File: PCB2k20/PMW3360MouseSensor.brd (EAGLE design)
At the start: 27 x 21 mm, 10 parts

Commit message: Make the screws not hit the lens
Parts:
- moved C3 4.49 mm to (20.6, 21.2)
- moved C4 4.49 mm to (23.1, 21.2)
- moved R3 4.49 mm to (13.0, 21.2)
- moved U$2 4.49 mm to (10.4, 13.0)
- moved R1 4.49 mm to (18.0, 21.2)
- moved R2 4.49 mm to (15.5, 21.2)
- moved U$1 3.42 mm to (3.43, 14.9)
- moved C2 3.42 mm to (2.79, 11.0)
- moved C1 3.42 mm to (5.33, 11.0)
- moved J1 3.17 mm to (4.70, 1.52)
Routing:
- net 3.3V: track 28.9 -> 34.8 mm
- net NRESET: track 21.5 -> 27.4 mm
- net N$42: track 39.1 -> 42.8 mm
- net N$46: track 3.89 -> 7.07 mm
- net N$47: track 3.83 -> 7.01 mm
- net N$45: track 4.69 -> 7.64 mm
- net N$40: track 6.21 -> 8.49 mm
- net 1.8V: track 22.5 -> 24.4 mm
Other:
- board size 27 x 21 mm -> 34.6 x 24 mm
- board text added: "todo: pin 1 marking pin label"

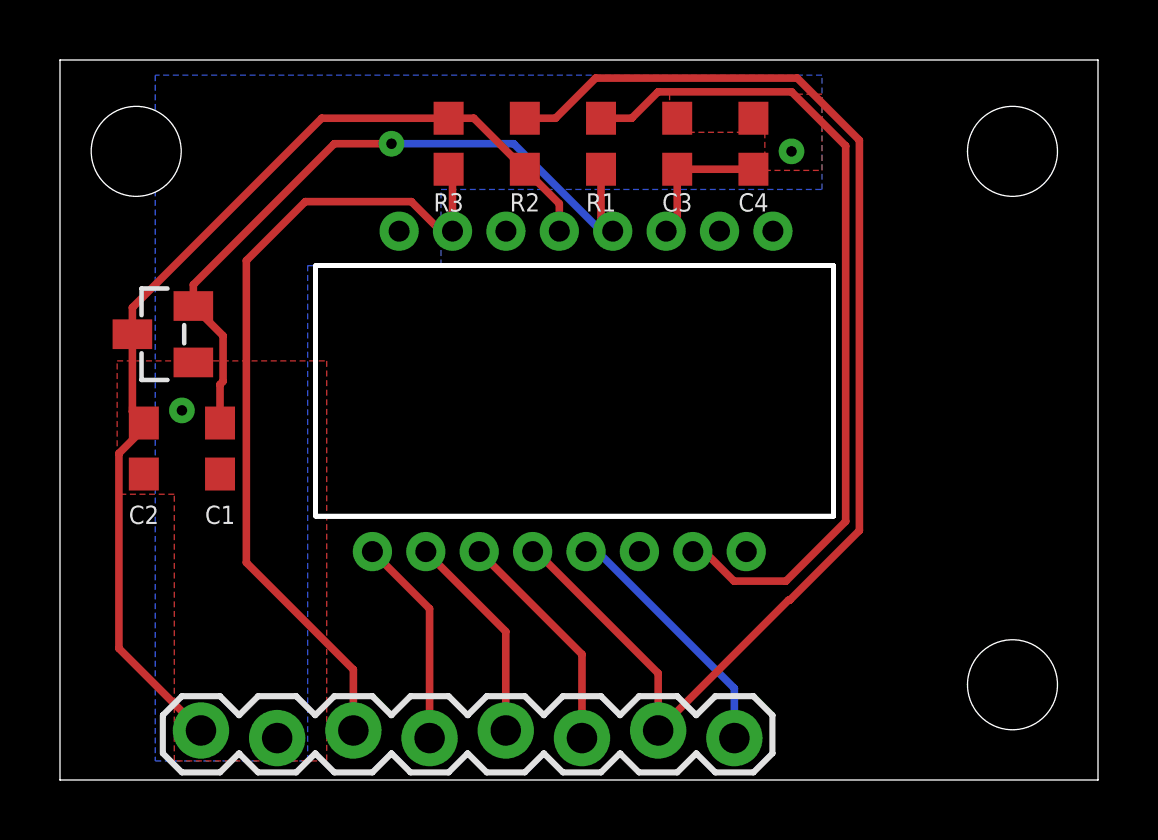
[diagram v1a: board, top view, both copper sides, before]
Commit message: Finalise PMW3360 breakout - done pin markings and cleanup - swapped position of some pins to route stuff more easily
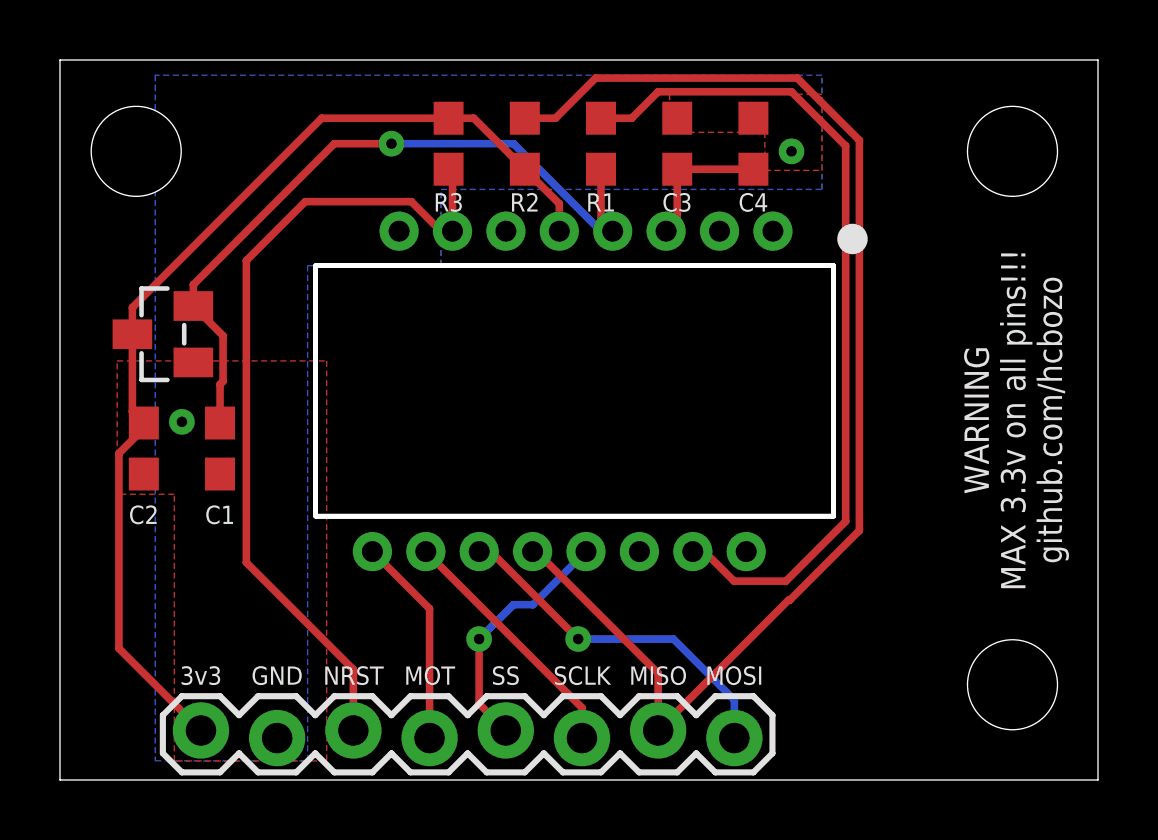
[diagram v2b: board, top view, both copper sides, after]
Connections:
- net N$42 renamed MISO
- net N$47 renamed MOT
- removed net N$40: J1.8, U$2.P13
- removed net N$45: J1.6, U$2.P11
- removed net N$46: J1.5, U$2.P10
- new net MOSI: J1.8, U$2.P11
- new net SCK: J1.6, U$2.P10
- new net SS: J1.5, U$2.P13
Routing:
- net MOSI: track 0.00 -> 11.8 mm, vias 0 -> 1
- net N$40: track 8.49 -> 0.00 mm
- net SCK: track 0.00 -> 8.37 mm
- net SS: track 0.00 -> 8.19 mm, vias 0 -> 1
- net N$45: track 7.64 -> 0.00 mm
- net N$46: track 7.07 -> 0.00 mm
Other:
- board text added: "3v3"
- board text added: "GND"
- board text added: "MISO"
- board text added: "MOSI"
- board text added: "MOT"
- board text added: "NRST"
- board text added: "SCLK"
- board text added: "SS"
- board text added: "WARNING MAX 3.3v on all pins!!! github.com/hcbozo"
- board text removed: "todo: pin 1 marking pin label"

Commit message: add gerbers, please everything turn out well!
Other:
- board text added: "WARNING MAX 3.3v on all pins!!! github.com/hcbozo PMW3360 Breakout"
- board text removed: "WARNING MAX 3.3v on all pins!!! github.com/hcbozo"
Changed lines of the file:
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@@
 <text x="33.401" y="12" size="0.8128" layer="21" font="vector" ratio="16" rot="R90" align="bottom-center">WARNING
 MAX 3.3v on all pins!!!
-github.com/hcbozo</text>
+github.com/hcbozo
+PMW3360 Breakout</text>
 </plain>
 <attributes>
